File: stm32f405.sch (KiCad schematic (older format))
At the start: 17 parts, among them Q1 CRYSTAL_50X32, U1 STM32F405R

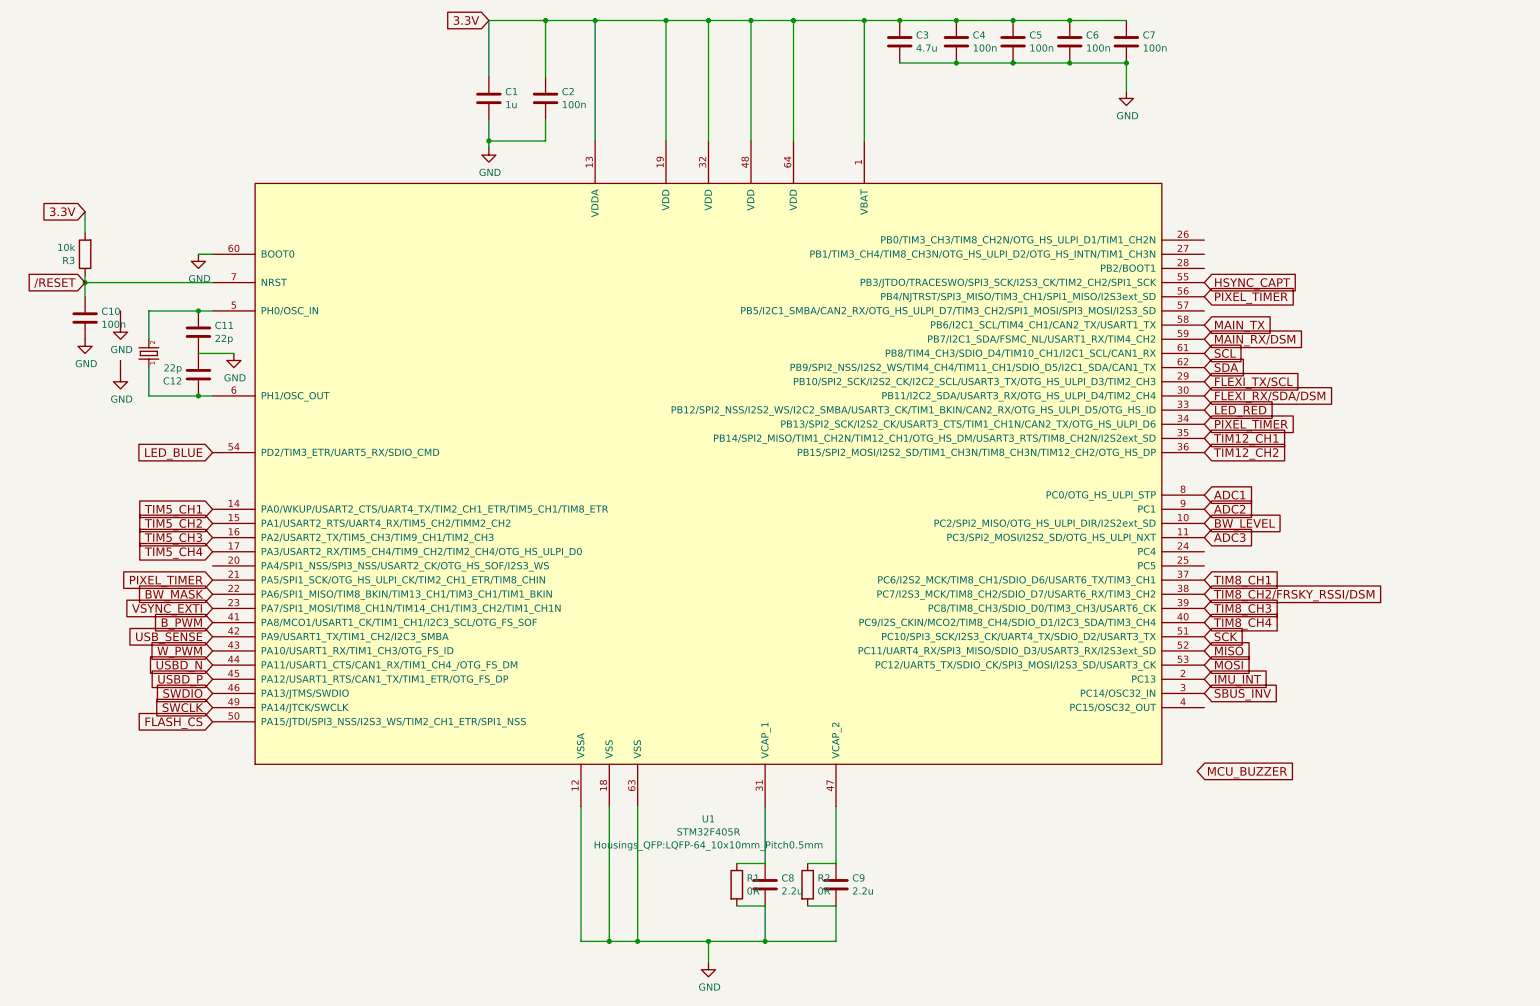
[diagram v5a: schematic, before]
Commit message: power traces routed
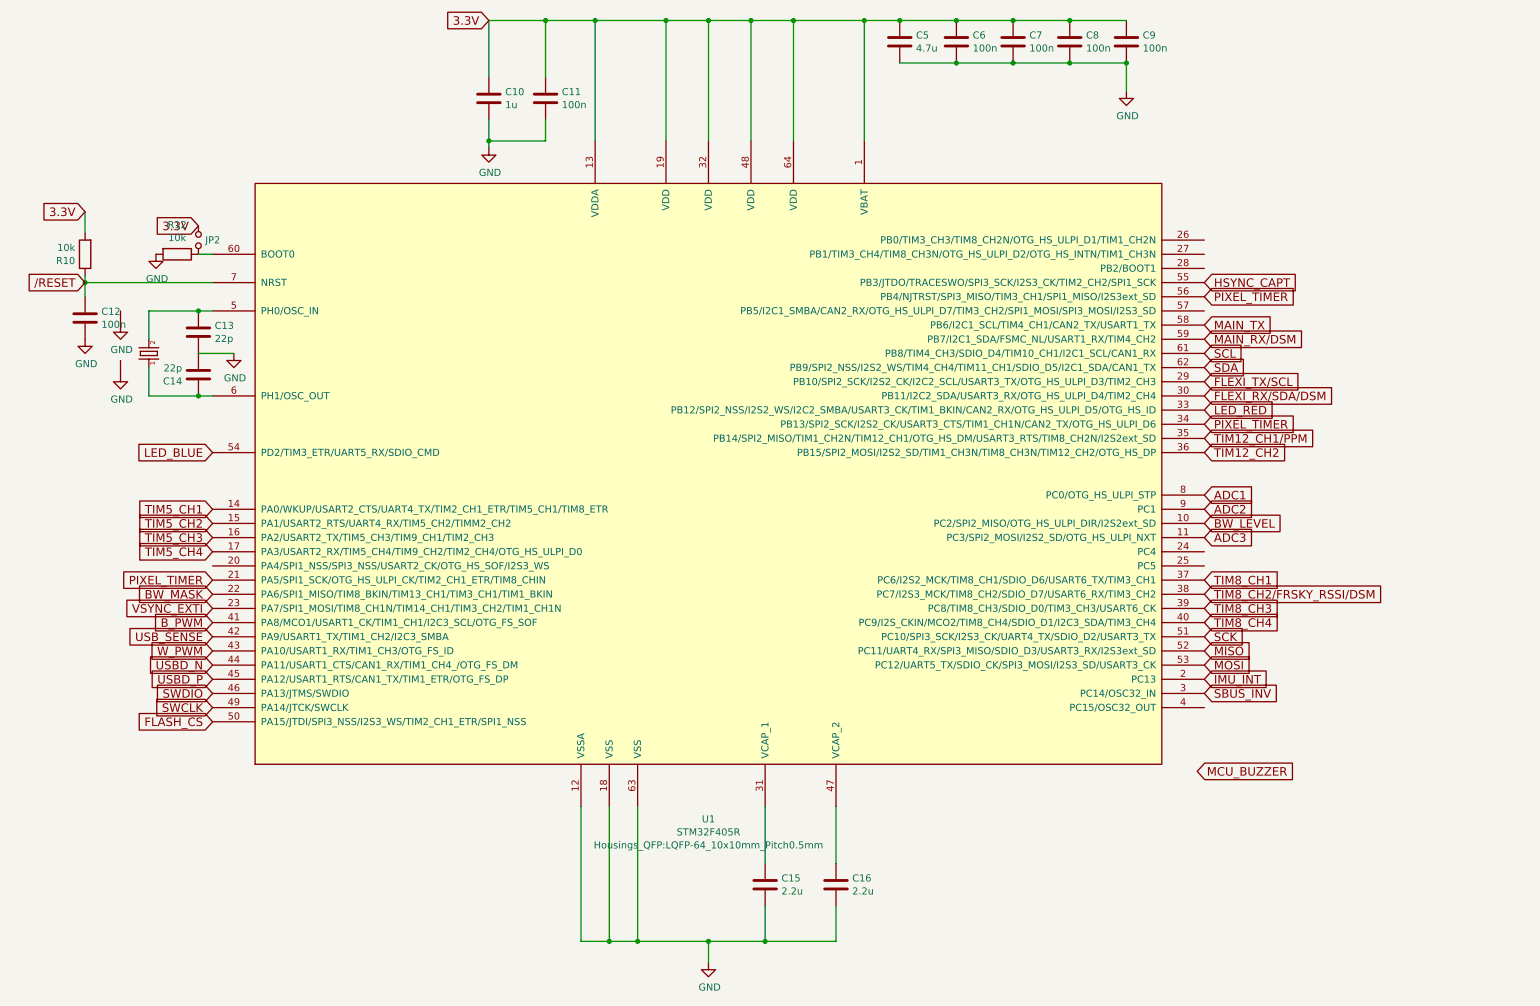
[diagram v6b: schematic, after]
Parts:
- removed R1, R2: 0R, Resistors_SMD:R_0402, symbol R
- added JP2: Jumper_NO_Small, minimal:ALIS-CUSTOM-PARTS_PAD-JUMPER-2-NO_YES_SILK, symbol Jumper_NO_Small
- added R12: 10k, Resistors_SMD:R_0603, symbol R
- C10: renamed from C1; footprint Capacitors_SMD:C_0402 -> Capacitors_SMD:C_0603
- C11: renamed from C2; footprint Capacitors_SMD:C_0402 -> Capacitors_SMD:C_0603
- C12: renamed from C10; footprint Capacitors_SMD:C_0402 -> Capacitors_SMD:C_0603
- C13: renamed from C11; footprint Capacitors_SMD:C_0402 -> Capacitors_SMD:C_0603
- C14: renamed from C12; footprint Capacitors_SMD:C_0402 -> Capacitors_SMD:C_0603
- C6: renamed from C4; footprint Capacitors_SMD:C_0402 -> Capacitors_SMD:C_0603
- C7: renamed from C5; footprint Capacitors_SMD:C_0402 -> Capacitors_SMD:C_0603
- C8: renamed from C6; footprint Capacitors_SMD:C_0402 -> Capacitors_SMD:C_0603
- C9: renamed from C7; footprint Capacitors_SMD:C_0402 -> Capacitors_SMD:C_0603
- R10: renamed from R3; footprint Resistors_SMD:R_0402 -> Resistors_SMD:R_0603
- renumbered C8 to C15, C9 to C16, C3 to C5, Q1 to Q6
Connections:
- net 3.3V: now also JP2.1
- net GND: now also R12.2; no longer U1.60 (BOOT0)
- net TIM12_CH1 renamed TIM12_CH1/PPM
- new net: JP2.2, R12.1, U1.60 (BOOT0)
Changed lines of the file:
@@
 $Descr A4 11693 8268
 encoding utf-8
-Sheet 4 7
+Sheet 3 8
 Title ""
 Date ""
@@
 ADC1
 Text GLabel 9050 3700 2    60   Input ~ 0
-TIM12_CH1
+TIM12_CH1/PPM
 Text GLabel 2050 4500 0    60   Input ~ 0
 TIM5_CH4
@@
 TIM5_CH2
 $Comp
-L C C4
+L C C6
 U 1 1 569AE236
 P 7300 900
-F 0 "C4" H 7415 946 50  0000 L CNN
+F 0 "C6" H 7415 946 50  0000 L CNN
 F 1 "100n" H 7415 854 50  0000 L CNN
-F 2 "Capacitors_SMD:C_0402" H 7338 750 50  0001 C CNN
+F 2 "Capacitors_SMD:C_0603" H 7338 750 50  0001 C CNN
 F 3 "" H 7300 900 50  0000 C CNN
 	1    7300 900
@@
 $EndComp
 $Comp
-L C C5
+L C C7
 U 1 1 569AE23D
 P 7700 900
-F 0 "C5" H 7815 946 50  0000 L CNN
+F 0 "C7" H 7815 946 50  0000 L CNN
 F 1 "100n" H 7815 854 50  0000 L CNN
-F 2 "Capacitors_SMD:C_0402" H 7738 750 50  0001 C CNN
+F 2 "Capacitors_SMD:C_0603" H 7738 750 50  0001 C CNN
 F 3 "" H 7700 900 50  0000 C CNN
 	1    7700 900
@@
 $EndComp
 $Comp
-L C C6
+L C C8
 U 1 1 569AE244
 P 8100 900
-F 0 "C6" H 8215 946 50  0000 L CNN
+F 0 "C8" H 8215 946 50  0000 L CNN
 F 1 "100n" H 8215 854 50  0000 L CNN
-F 2 "Capacitors_SMD:C_0402" H 8138 750 50  0001 C CNN
+F 2 "Capacitors_SMD:C_0603" H 8138 750 50  0001 C CNN
 F 3 "" H 8100 900 50  0000 C CNN
 	1    8100 900
@@
 $EndComp
 $Comp
-L C C7
+L C C9
 U 1 1 569AE24B
 P 8500 900
-F 0 "C7" H 8615 946 50  0000 L CNN
+F 0 "C9" H 8615 946 50  0000 L CNN
 F 1 "100n" H 8615 854 50  0000 L CNN
-F 2 "Capacitors_SMD:C_0402" H 8538 750 50  0001 C CNN
+F 2 "Capacitors_SMD:C_0603" H 8538 750 50  0001 C CNN
 F 3 "" H 8500 900 50  0000 C CNN
 	1    8500 900
@@
 $EndComp
 $Comp
-L C C3
+L C C5
 U 1 1 569AE252
 P 6900 900
-F 0 "C3" H 7015 946 50  0000 L CNN
+F 0 "C5" H 7015 946 50  0000 L CNN
 F 1 "4.7u" H 7015 854 50  0000 L CNN
 F 2 "Capacitors_SMD:C_0805" H 6938 750 50  0001 C CNN
@@
 $EndComp
 $Comp
-L GND #PWR020
+L GND #PWR010
 U 1 1 569AE259
 P 5550 7400
-F 0 "#PWR020" H 5550 7150 50  0001 C CNN
+F 0 "#PWR010" H 5550 7150 50  0001 C CNN
 F 1 "GND" H 5558 7226 50  0000 C CNN
 F 2 "" H 5550 7400 50  0000 C CNN
@@
 $EndComp
 $Comp
-L C C8
+L C C15
 U 1 1 569AE25F
 P 5950 6850
-F 0 "C8" H 6065 6896 50  0000 L CNN
+F 0 "C15" H 6065 6896 50  0000 L CNN
 F 1 "2.2u" H 6065 6804 50  0000 L CNN
 F 2 "Capacitors_SMD:C_0603" H 5988 6700 50  0001 C CNN
@@
 $EndComp
 $Comp
-L C C9
+L C C16
 U 1 1 569AE266
 P 6450 6850
-F 0 "C9" H 6565 6896 50  0000 L CNN
+F 0 "C16" H 6565 6896 50  0000 L CNN
 F 1 "2.2u" H 6565 6804 50  0000 L CNN
 F 2 "Capacitors_SMD:C_0603" H 6488 6700 50  0001 C CNN
@@
 $EndComp
 $Comp
-L C C2
+L C C11
 U 1 1 569AE26D
 P 4400 1300
-F 0 "C2" H 4515 1346 50  0000 L CNN
+F 0 "C11" H 4515 1346 50  0000 L CNN
 F 1 "100n" H 4515 1254 50  0000 L CNN
-F 2 "Capacitors_SMD:C_0402" H 4438 1150 50  0001 C CNN
+F 2 "Capacitors_SMD:C_0603" H 4438 1150 50  0001 C CNN
 F 3 "" H 4400 1300 50  0000 C CNN
 	1    4400 1300
@@
 $EndComp
 $Comp
-L C C1
+L C C10
 U 1 1 569AE274
 P 4000 1300
-F 0 "C1" H 4115 1346 50  0000 L CNN
+F 0 "C10" H 4115 1346 50  0000 L CNN
 F 1 "1u" H 4115 1254 50  0000 L CNN
-F 2 "Capacitors_SMD:C_0402" H 4038 1150 50  0001 C CNN
+F 2 "Capacitors_SMD:C_0603" H 4038 1150 50  0001 C CNN
 F 3 "" H 4000 1300 50  0000 C CNN
 	1    4000 1300
@@
 $EndComp
 $Comp
-L GND #PWR021
+L GND #PWR011
 U 1 1 569AE27B
 P 4000 1650
-F 0 "#PWR021" H 4000 1400 50  0001 C CNN
+F 0 "#PWR011" H 4000 1400 50  0001 C CNN
 F 1 "GND" H 4008 1476 50  0000 C CNN
 F 2 "" H 4000 1650 50  0000 C CNN
@@
 	1    0    0    -1
 $EndComp
-$Comp
-L R R1
-U 1 1 569AE281
-P 5750 6850
-F 0 "R1" H 5820 6896 50  0000 L CNN
-F 1 "0R" H 5820 6804 50  0000 L CNN
-F 2 "Resistors_SMD:R_0402" V 5680 6850 50  0001 C CNN
-F 3 "" H 5750 6850 50  0000 C CNN
-	1    5750 6850
-	1    0    0    -1
-$EndComp
-$Comp
-L R R2
-U 1 1 569AE288
-P 6250 6850
-F 0 "R2" H 6320 6896 50  0000 L CNN
-F 1 "0R" H 6320 6804 50  0000 L CNN
-F 2 "Resistors_SMD:R_0402" V 6180 6850 50  0001 C CNN
-F 3 "" H 6250 6850 50  0000 C CNN
-	1    6250 6850
-	1    0    0    -1
-$EndComp
 Text GLabel 1150 2100 0    60   Input ~ 0
 3.3V
 $Comp
-L R R3
+L R R10
 U 1 1 569AE291
 P 1150 2400
-F 0 "R3" H 1220 2446 50  0000 L CNN
+F 0 "R10" H 1220 2446 50  0000 L CNN
 F 1 "10k" H 1220 2354 50  0000 L CNN
-F 2 "Resistors_SMD:R_0402" V 1080 2400 50  0001 C CNN
+F 2 "Resistors_SMD:R_0603" V 1080 2400 50  0001 C CNN
 F 3 "" H 1150 2400 50  0000 C CNN
 	1    1150 2400
@@
 $EndComp
 $Comp
-L C C10
+L C C12
 U 1 1 569AE298
 P 1150 2850
-F 0 "C10" H 1265 2896 50  0000 L CNN
+F 0 "C12" H 1265 2896 50  0000 L CNN
 F 1 "100n" H 1265 2804 50  0000 L CNN
-F 2 "Capacitors_SMD:C_0402" H 1188 2700 50  0001 C CNN
+F 2 "Capacitors_SMD:C_0603" H 1188 2700 50  0001 C CNN
 F 3 "" H 1150 2850 50  0000 C CNN
 	1    1150 2850
@@
 $EndComp
 $Comp
-L GND #PWR022
+L GND #PWR012
 U 1 1 569AE29F
 P 1150 3000
-F 0 "#PWR022" H 1150 2750 50  0001 C CNN
+F 0 "#PWR012" H 1150 2750 50  0001 C CNN
 F 1 "GND" H 1158 2826 50  0000 C CNN
 F 2 "" H 1150 3000 50  0000 C CNN
@@
 P 1600 3100
 AR Path="/569AE2A5" Ref="Q?"  Part="3"
-AR Path="/56980F8D/569AE2A5" Ref="Q1"  Part="3"
-F 0 "Q1" H 1600 3100 50  0001 C CNN
+AR Path="/56980F8D/569AE2A5" Ref="Q6"  Part="3"
+F 0 "Q6" H 1600 3100 50  0001 C CNN
 F 1 "CRYSTAL_50X32" H 1600 3100 50  0001 C CNN
 F 2 "minimal:CRYSTAL_50X32" H 1630 3250 20  0001 C CNN
@@
 P 1400 2800
 AR Path="/569AE2AB" Ref="Q?"  Part="2"
-AR Path="/56980F8D/569AE2AB" Ref="Q1"  Part="2"
-F 0 "Q1" H 1400 2800 50  0001 C CNN
+AR Path="/56980F8D/569AE2AB" Ref="Q6"  Part="2"
+F 0 "Q6" H 1400 2800 50  0001 C CNN
 F 1 "CRYSTAL_50X32" H 1400 2800 50  0001 C CNN
 F 2 "minimal:CRYSTAL_50X32" H 1430 2950 20  0001 C CNN
@@
 P 1400 3150
 AR Path="/569AE2B1" Ref="Q?"  Part="1"
-AR Path="/56980F8D/569AE2B1" Ref="Q1"  Part="1"
-F 0 "Q1" H 1400 3150 50  0001 C CNN
+AR Path="/56980F8D/569AE2B1" Ref="Q6"  Part="1"
+F 0 "Q6" H 1400 3150 50  0001 C CNN
 F 1 "CRYSTAL_50X32" H 1400 3150 50  0001 C CNN
 F 2 "minimal:CRYSTAL_50X32" H 1430 3300 20  0001 C CNN
@@
 $EndComp
 $Comp
-L GND #PWR023
+L GND #PWR013
 U 1 1 569AE2B7
 P 1400 2900
-F 0 "#PWR023" H 1400 2650 50  0001 C CNN
+F 0 "#PWR013" H 1400 2650 50  0001 C CNN
 F 1 "GND" H 1408 2726 50  0000 C CNN
 F 2 "" H 1400 2900 50  0000 C CNN
@@
 $EndComp
 $Comp
-L GND #PWR024
+L GND #PWR014
 U 1 1 569AE2BD
 P 1400 3250
-F 0 "#PWR024" H 1400 3000 50  0001 C CNN
+F 0 "#PWR014" H 1400 3000 50  0001 C CNN
 F 1 "GND" H 1408 3076 50  0000 C CNN
 F 2 "" H 1400 3250 50  0000 C CNN
@@
 $EndComp
 $Comp
-L C C11
+L C C13
 U 1 1 569AE2C3
 P 1950 2950
-F 0 "C11" H 2065 2996 50  0000 L CNN
+F 0 "C13" H 2065 2996 50  0000 L CNN
 F 1 "22p" H 2065 2904 50  0000 L CNN
-F 2 "Capacitors_SMD:C_0402" H 1988 2800 50  0001 C CNN
+F 2 "Capacitors_SMD:C_0603" H 1988 2800 50  0001 C CNN
 F 3 "" H 1950 2950 50  0000 C CNN
 	1    1950 2950
@@
 $EndComp
 $Comp
-L C C12
+L C C14
 U 1 1 569AE2CA
 P 1950 3250
-F 0 "C12" H 2065 3296 50  0000 L CNN
+F 0 "C14" H 2065 3296 50  0000 L CNN
 F 1 "22p" H 2065 3204 50  0000 L CNN
-F 2 "Capacitors_SMD:C_0402" H 1988 3100 50  0001 C CNN
+F 2 "Capacitors_SMD:C_0603" H 1988 3100 50  0001 C CNN
 F 3 "" H 1950 3250 50  0000 C CNN
 	1    1950 3250
@@
 $EndComp
 $Comp
-L GND #PWR025
+L GND #PWR015
 U 1 1 569AE2D1
 P 2200 3100
-F 0 "#PWR025" H 2200 2850 50  0001 C CNN
+F 0 "#PWR015" H 2200 2850 50  0001 C CNN
 F 1 "GND" H 2208 2926 50  0000 C CNN
 F 2 "" H 2200 3100 50  0000 C CNN
@@
 	4000 750  8500 750
 $Comp
-L GND #PWR026
+L GND #PWR016
 U 1 1 569E1F9F
-P 1950 2400
-F 0 "#PWR026" H 1950 2150 50  0001 C CNN
-F 1 "GND" H 1958 2226 50  0000 C CNN
-F 2 "" H 1950 2400 50  0000 C CNN
-F 3 "" H 1950 2400 50  0000 C CNN
-	1    1950 2400
+P 1650 2400
+F 0 "#PWR016" H 1650 2150 50  0001 C CNN
+F 1 "GND" H 1658 2226 50  0000 C CNN
+F 2 "" H 1650 2400 50  0000 C CNN
+F 3 "" H 1650 2400 50  0000 C CNN
+	1    1650 2400
 	1    0    0    -1
 $EndComp
@@
 Wire Wire Line
 	5950 6300 5950 6700
-Wire Wire Line
-	5950 6700 5750 6700
-Wire Wire Line
-	5750 7000 5950 7000
-Wire Wire Line
-	6250 7000 6450 7000
-Wire Wire Line
-	6450 6700 6250 6700
 Wire Wire Line
 	6450 6300 6450 6700
@@
 Connection ~ 6900 750
 $Comp
-L GND #PWR027
+L GND #PWR017
 U 1 1 569E5F3D
 P 8500 1250
-F 0 "#PWR027" H 8500 1000 50  0001 C CNN
+F 0 "#PWR017" H 8500 1000 50  0001 C CNN
 F 1 "GND" H 8508 1076 50  0000 C CNN
 F 2 "" H 8500 1250 50  0000 C CNN
@@
 Text GLabel 2050 5200 0    60   Input ~ 0
 W_PWM
+$Comp
+L Jumper_NO_Small JP2
+U 1 1 5729B83C
+P 1950 2300
+F 0 "JP2" V 1950 2348 50  0000 L CNN
+F 1 "Jumper_NO_Small" H 1960 2240 50  0001 C CNN
+F 2 "minimal:ALIS-CUSTOM-PARTS_PAD-JUMPER-2-NO_YES_SILK" H 1950 2300 50  0001 C CNN
+F 3 "" H 1950 2300 50  0000 C CNN
+	1    1950 2300
+	0    1    1    0
+$EndComp
+$Comp
+L R R12
+U 1 1 5729B8D0
+P 1800 2400
+F 0 "R12" V 1593 2400 50  0000 C CNN
+F 1 "10k" V 1684 2400 50  0000 C CNN
+F 2 "Resistors_SMD:R_0603" V 1730 2400 50  0001 C CNN
+F 3 "" H 1800 2400 50  0000 C CNN
+	1    1800 2400
+	0    1    1    0
+$EndComp
+Text GLabel 1950 2200 0    60   Input ~ 0
+3.3V
 $EndSCHEMATC

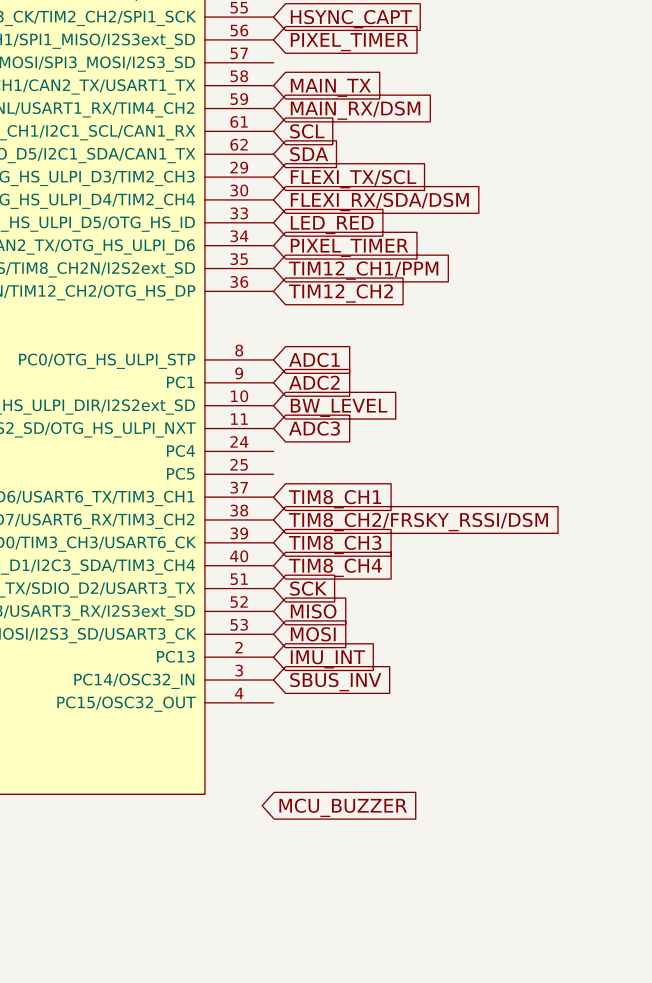
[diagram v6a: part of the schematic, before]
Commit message: best relative placement
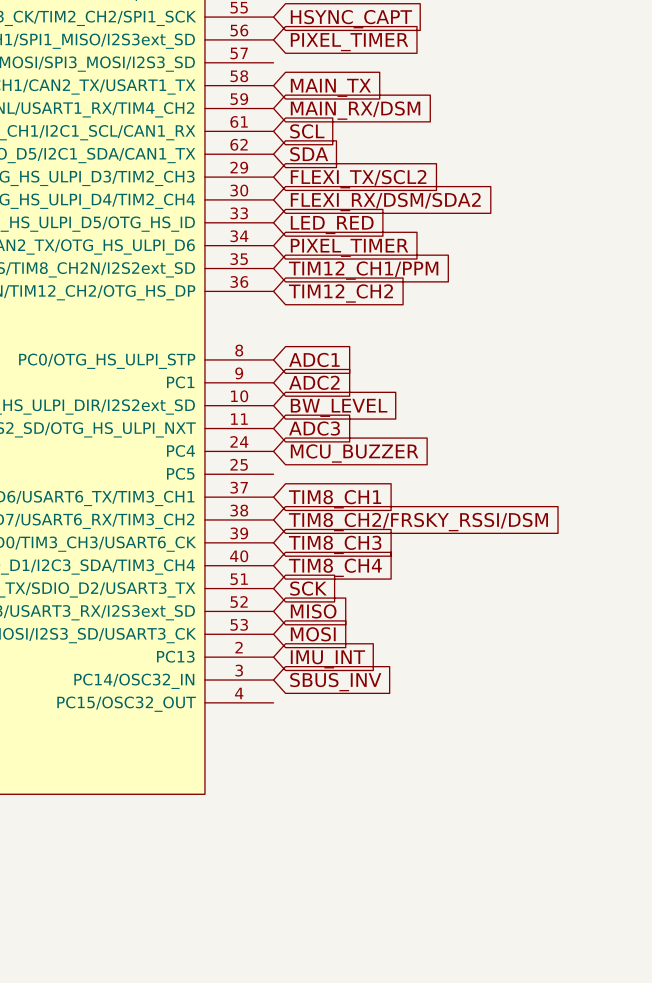
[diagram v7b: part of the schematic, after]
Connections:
- net MCU_BUZZER: now also U1.24 (PC4)
- net FLEXI_RX/SDA/DSM renamed FLEXI_RX/DSM/SDA2
- net FLEXI_TX/SCL renamed FLEXI_TX/SCL2
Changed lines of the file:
@@
 SBUS_INV
 Text GLabel 9050 3300 2    60   Input ~ 0
-FLEXI_TX/SCL
+FLEXI_TX/SCL2
 Text GLabel 9050 3000 2    60   Input ~ 0
 MAIN_RX/DSM
 Text GLabel 9050 3400 2    60   Input ~ 0
-FLEXI_RX/SDA/DSM
+FLEXI_RX/DSM/SDA2
 Text GLabel 9050 3100 2    60   Input ~ 0
 SCL
@@
 Text GLabel 1150 2600 0    60   Input ~ 0
 /RESET
-Text GLabel 9000 6050 2    60   Input ~ 0
+Text GLabel 9050 4500 2    60   Input ~ 0
 MCU_BUZZER
 Text GLabel 9050 3800 2    60   Input ~ 0

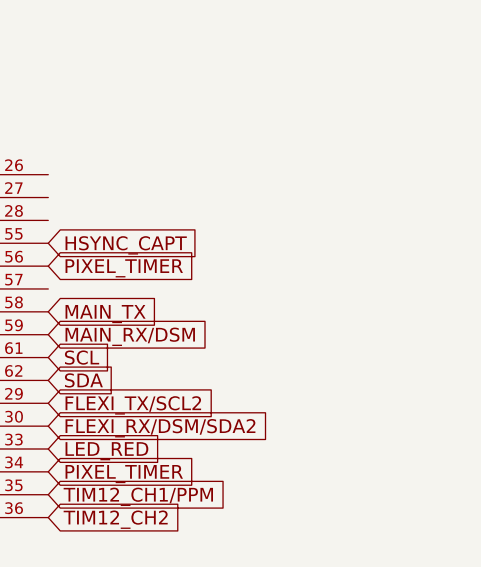
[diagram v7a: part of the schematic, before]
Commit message: added I2C pullups and pulled MPU6050 AD0 to GND (DOH)
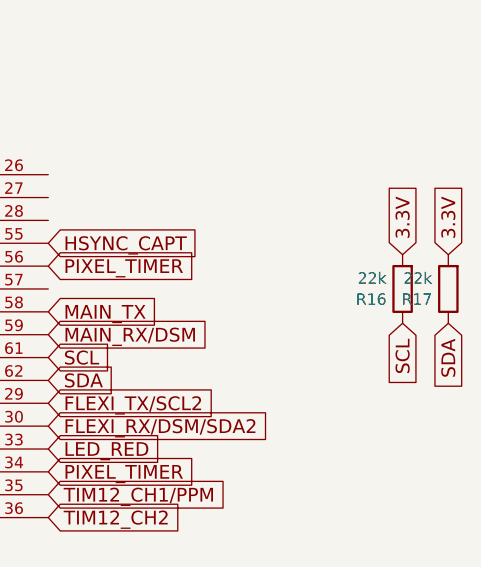
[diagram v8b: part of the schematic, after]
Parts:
- added R16, R17: 22k, Resistors_SMD:R_0603, symbol R
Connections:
- net 3.3V: now also R16.2, R17.2
- net SCL: now also R16.1
- net SDA: now also R17.1
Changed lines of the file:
@@
 Text GLabel 1950 2200 0    60   Input ~ 0
 3.3V
+$Comp
+L R R17
+U 1 1 5735F274
+P 10800 2800
+F 0 "R17" H 10870 2846 50  0000 L CNN
+F 1 "22k" H 10870 2754 50  0000 L CNN
+F 2 "Resistors_SMD:R_0603" V 10730 2800 50  0001 C CNN
+F 3 "" H 10800 2800 50  0000 C CNN
+	1    10800 2800
+	-1   0    0    1
+$EndComp
+$Comp
+L R R16
+U 1 1 5735F9C6
+P 10600 2800
+F 0 "R16" H 10670 2846 50  0000 L CNN
+F 1 "22k" H 10670 2754 50  0000 L CNN
+F 2 "Resistors_SMD:R_0603" V 10530 2800 50  0001 C CNN
+F 3 "" H 10600 2800 50  0000 C CNN
+	1    10600 2800
+	-1   0    0    1
+$EndComp
+Text GLabel 10600 2950 3    60   Input ~ 0
+SCL
+Text GLabel 10800 2950 3    60   Input ~ 0
+SDA
+Text GLabel 10600 2650 1    60   Input ~ 0
+3.3V
+Text GLabel 10800 2650 1    60   Input ~ 0
+3.3V
 $EndSCHEMATC
